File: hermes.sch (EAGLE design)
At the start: 17 parts, among them IC1 LP5912-WSON-6

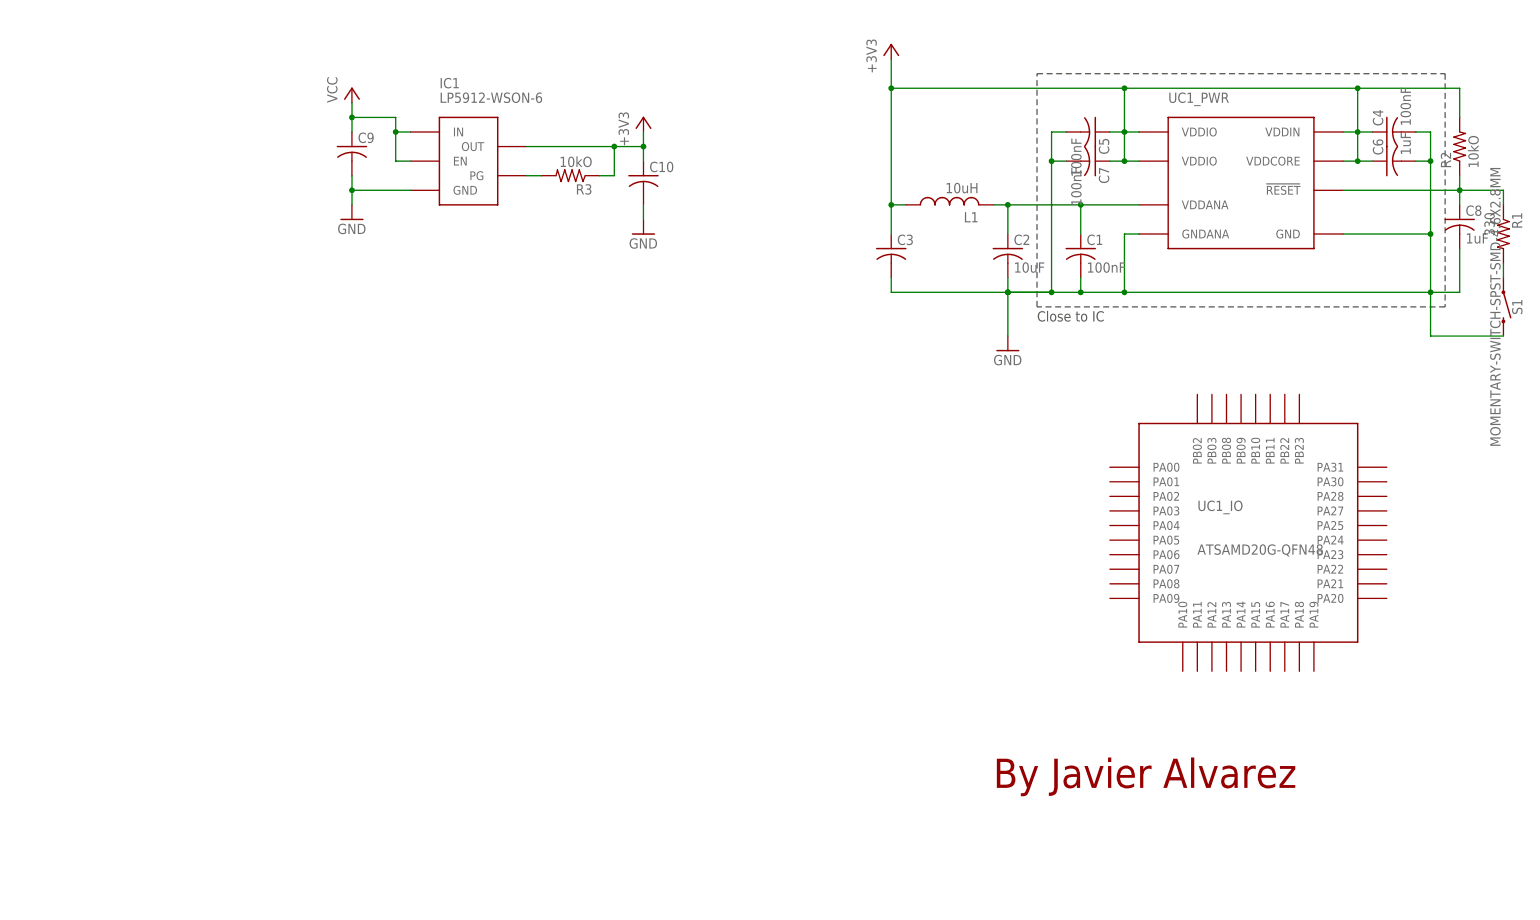
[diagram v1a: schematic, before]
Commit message: -SCH: Add placeholders for XTAL and LED -LBR: Add symbolic connection
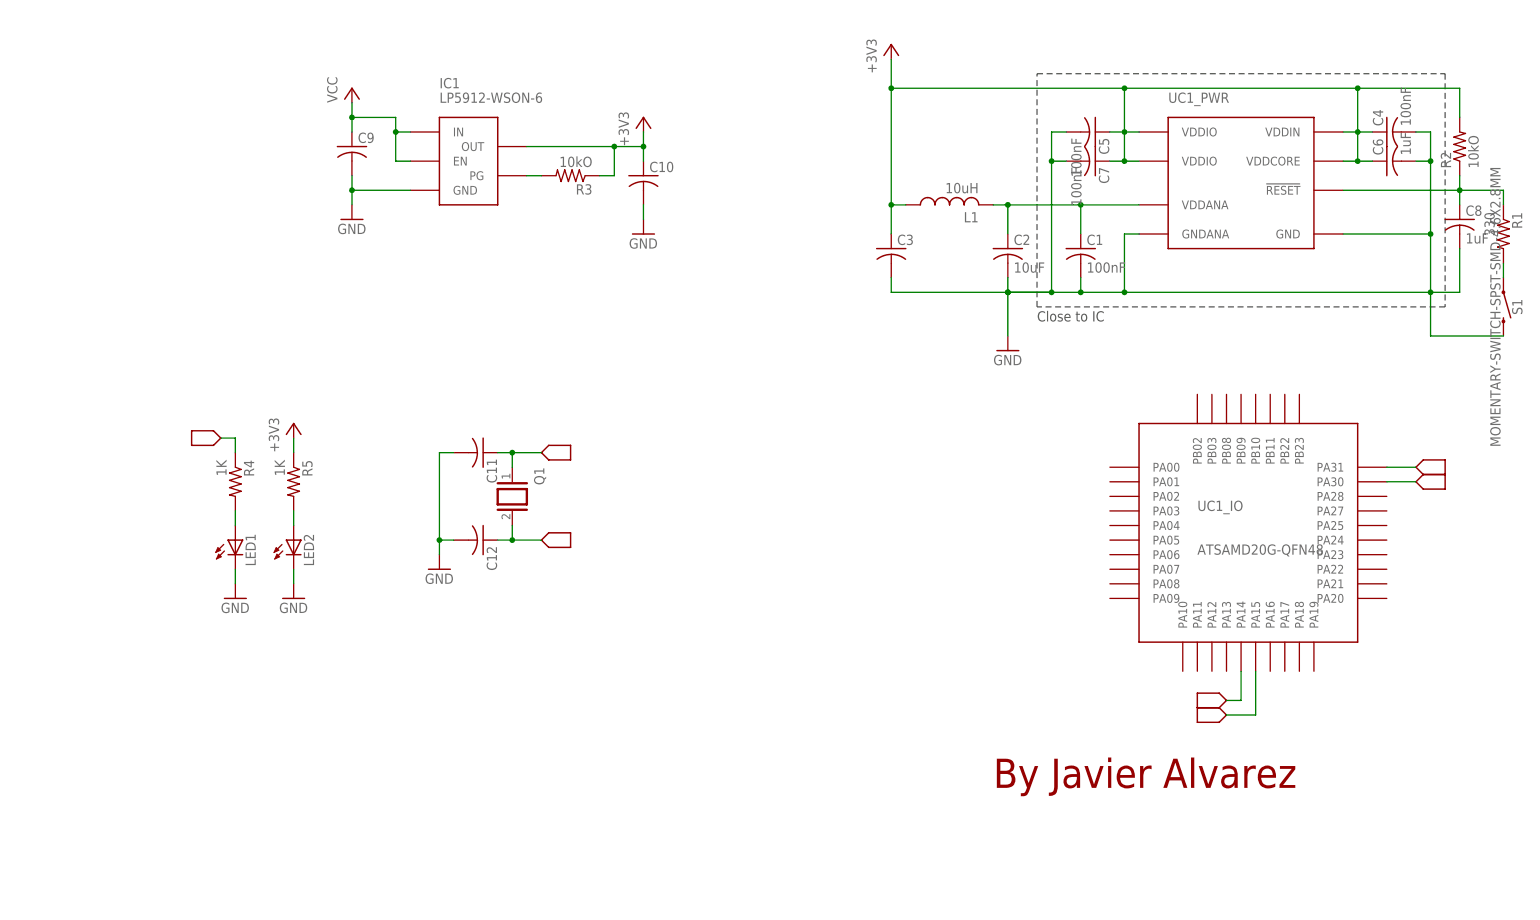
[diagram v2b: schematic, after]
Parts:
- added C11, C12: (no value), rcl:C-USC0201
- added LED1, LED2: (no value), eagle-ltspice:LED_ESML0603
- added Q1: (no value), special:XTAL
- added R4, R5: 1K, rcl:R-US_R0201
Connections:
- new net LED: R4.1
- new net N$6: LED1.A, R4.2
- new net N$7: LED2.A, R5.2
- new net SWCLK: UC1_IO.PA30
- new net SWDIO: UC1_IO.PA31
- new net XIN: C11.1, Q1.1, UC1_IO.PA14
- new net XOUT: C12.1, Q1.2, UC1_IO.PA15
- net +3V3: now also R5.1
- net GND: now also C11.2, C12.2, LED1.C, LED2.C
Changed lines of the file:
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@@
 <?xml version="1.0" encoding="utf-8"?>
 <!DOCTYPE eagle SYSTEM "eagle.dtd">
-<eagle version="8.3.0">
+<eagle version="8.5.0">
 <drawing>
 <settings>
@@
 <layer number="94" name="Symbols" color="4" fill="1" visible="yes" active="yes"/>
 <layer number="95" name="Names" color="7" fill="1" visible="yes" active="yes"/>
-<layer number="96" name="Values" color="7" fill="1" visible="no" active="yes"/>
+<layer number="96" name="Values" color="7" fill="1" visible="yes" active="yes"/>
 <layer number="97" name="Info" color="7" fill="1" visible="yes" active="yes"/>
 <layer number="98" name="Guide" color="6" fill="1" visible="yes" active="yes"/>
@@
 <part name="GND3" library="supply1" library_urn="urn:adsk.eagle:library:371" deviceset="GND" device=""/>
 <part name="+3V2" library="supply1" library_urn="urn:adsk.eagle:library:371" deviceset="+3V3" device=""/>
+<part name="U$1" library="Hermes_lib" deviceset="NET_CON" device=""/>
+<part name="LED1" library="eagle-ltspice" library_urn="urn:adsk.eagle:library:217" deviceset="LED_E" device="SML0603" package3d_urn="urn:adsk.eagle:package:13315/1"/>
+<part name="LED2" library="eagle-ltspice" library_urn="urn:adsk.eagle:library:217" deviceset="LED_E" device="SML0603" package3d_urn="urn:adsk.eagle:package:13315/1"/>
+<part name="R4" library="rcl" library_urn="urn:adsk.eagle:library:334" deviceset="R-US_" device="R0201" package3d_urn="urn:adsk.eagle:package:23593/1" value="1K"/>
+<part name="R5" library="rcl" library_urn="urn:adsk.eagle:library:334" deviceset="R-US_" device="R0201" package3d_urn="urn:adsk.eagle:package:23593/1" value="1K"/>
+<part name="+3V3" library="supply1" library_urn="urn:adsk.eagle:library:371" deviceset="+3V3" device=""/>
+<part name="GND4" library="supply1" library_urn="urn:adsk.eagle:library:371" deviceset="GND" device=""/>
+<part name="GND5" library="supply1" library_urn="urn:adsk.eagle:library:371" deviceset="GND" device=""/>
+<part name="Q1" library="special" library_urn="urn:adsk.eagle:library:367" deviceset="XTAL" device="" package3d_urn="urn:adsk.eagle:package:26649/1"/>
+<part name="U$2" library="Hermes_lib" deviceset="NET_CON" device=""/>
+<part name="U$3" library="Hermes_lib" deviceset="NET_CON" device=""/>
+<part name="C11" library="rcl" library_urn="urn:adsk.eagle:library:334" deviceset="C-US" device="C0201" package3d_urn="urn:adsk.eagle:package:23690/1"/>
+<part name="C12" library="rcl" library_urn="urn:adsk.eagle:library:334" deviceset="C-US" device="C0201" package3d_urn="urn:adsk.eagle:package:23690/1"/>
+<part name="GND6" library="supply1" library_urn="urn:adsk.eagle:library:371" deviceset="GND" device=""/>
+<part name="U$4" library="Hermes_lib" deviceset="NET_CON" device=""/>
+<part name="U$5" library="Hermes_lib" deviceset="NET_CON" device=""/>
+<part name="U$6" library="Hermes_lib" deviceset="NET_CON" device=""/>
+<part name="U$7" library="Hermes_lib" deviceset="NET_CON" device=""/>
 </parts>
 <sheets>
@@
 <instance part="GND3" gate="1" x="55.88" y="127"/>
 <instance part="+3V2" gate="G$1" x="106.68" y="144.78"/>
+<instance part="U$1" gate="G$1" x="33.02" y="88.9" rot="R180"/>
+<instance part="LED1" gate="G$1" x="35.56" y="71.12"/>
+<instance part="LED2" gate="G$1" x="45.72" y="71.12"/>
+<instance part="R4" gate="G$1" x="35.56" y="81.28" rot="R270"/>
+<instance part="R5" gate="G$1" x="45.72" y="81.28" rot="R270"/>
+<instance part="+3V3" gate="G$1" x="45.72" y="91.44"/>
+<instance part="GND4" gate="1" x="45.72" y="60.96"/>
+<instance part="GND5" gate="1" x="35.56" y="60.96"/>
+<instance part="Q1" gate="G$1" x="83.82" y="78.74" rot="R270"/>
+<instance part="U$2" gate="G$1" x="88.9" y="86.36"/>
+<instance part="U$3" gate="G$1" x="88.9" y="71.12"/>
+<instance part="C11" gate="G$1" x="78.74" y="86.36" rot="R270"/>
+<instance part="C12" gate="G$1" x="78.74" y="71.12" rot="R270"/>
+<instance part="GND6" gate="1" x="71.12" y="66.04"/>
+<instance part="U$4" gate="G$1" x="208.28" y="43.18" rot="R180"/>
+<instance part="U$5" gate="G$1" x="208.28" y="40.64" rot="R180"/>
+<instance part="U$6" gate="G$1" x="241.3" y="83.82"/>
+<instance part="U$7" gate="G$1" x="241.3" y="81.28"/>
 </instances>
 <busses>
@@
 <wire x1="106.68" y1="142.24" x2="106.68" y2="139.7" width="0.1524" layer="91"/>
 <junction x="106.68" y="139.7"/>
+</segment>
+<segment>
+<pinref part="R5" gate="G$1" pin="1"/>
+<pinref part="+3V3" gate="G$1" pin="+3V3"/>
+<wire x1="45.72" y1="86.36" x2="45.72" y2="88.9" width="0.1524" layer="91"/>
 </segment>
 </net>
@@
 <junction x="55.88" y="132.08"/>
 </segment>
+<segment>
+<pinref part="GND5" gate="1" pin="GND"/>
+<pinref part="LED1" gate="G$1" pin="C"/>
+<wire x1="35.56" y1="63.5" x2="35.56" y2="66.04" width="0.1524" layer="91"/>
+</segment>
+<segment>
+<pinref part="GND4" gate="1" pin="GND"/>
+<pinref part="LED2" gate="G$1" pin="C"/>
+<wire x1="45.72" y1="63.5" x2="45.72" y2="66.04" width="0.1524" layer="91"/>
+</segment>
+<segment>
+<pinref part="C11" gate="G$1" pin="2"/>
+<wire x1="73.66" y1="86.36" x2="71.12" y2="86.36" width="0.1524" layer="91"/>
+<wire x1="71.12" y1="86.36" x2="71.12" y2="71.12" width="0.1524" layer="91"/>
+<pinref part="C12" gate="G$1" pin="2"/>
+<wire x1="71.12" y1="71.12" x2="73.66" y2="71.12" width="0.1524" layer="91"/>
+<pinref part="GND6" gate="1" pin="GND"/>
+<wire x1="71.12" y1="68.58" x2="71.12" y2="71.12" width="0.1524" layer="91"/>
+<junction x="71.12" y="71.12"/>
+</segment>
 </net>
 <net name="N$2" class="0">
@@
 </segment>
 </net>
+<net name="LED" class="0">
+<segment>
+<pinref part="R4" gate="G$1" pin="1"/>
+<wire x1="35.56" y1="86.36" x2="35.56" y2="88.9" width="0.1524" layer="91"/>
+<wire x1="35.56" y1="88.9" x2="33.02" y2="88.9" width="0.1524" layer="91"/>
+</segment>
+</net>
+<net name="N$6" class="0">
+<segment>
+<pinref part="LED1" gate="G$1" pin="A"/>
+<pinref part="R4" gate="G$1" pin="2"/>
+<wire x1="35.56" y1="73.66" x2="35.56" y2="76.2" width="0.1524" layer="91"/>
+</segment>
+</net>
+<net name="N$7" class="0">
+<segment>
+<pinref part="LED2" gate="G$1" pin="A"/>
+<pinref part="R5" gate="G$1" pin="2"/>
+<wire x1="45.72" y1="73.66" x2="45.72" y2="76.2" width="0.1524" layer="91"/>
+</segment>
+</net>
+<net name="XIN" class="0">
+<segment>
+<pinref part="Q1" gate="G$1" pin="1"/>
+<wire x1="83.82" y1="86.36" x2="83.82" y2="83.82" width="0.1524" layer="91"/>
+<pinref part="C11" gate="G$1" pin="1"/>
+<wire x1="81.28" y1="86.36" x2="83.82" y2="86.36" width="0.1524" layer="91"/>
+<junction x="83.82" y="86.36"/>
+<wire x1="88.9" y1="86.36" x2="83.82" y2="86.36" width="0.1524" layer="91"/>
+</segment>
+<segment>
+<pinref part="UC1" gate="_IO" pin="PA14"/>
+<wire x1="210.82" y1="48.26" x2="210.82" y2="43.18" width="0.1524" layer="91"/>
+<wire x1="210.82" y1="43.18" x2="208.28" y2="43.18" width="0.1524" layer="91"/>
+</segment>
+</net>
+<net name="XOUT" class="0">
+<segment>
+<pinref part="Q1" gate="G$1" pin="2"/>
+<wire x1="88.9" y1="71.12" x2="83.82" y2="71.12" width="0.1524" layer="91"/>
+<wire x1="83.82" y1="71.12" x2="83.82" y2="73.66" width="0.1524" layer="91"/>
+<pinref part="C12" gate="G$1" pin="1"/>
+<wire x1="81.28" y1="71.12" x2="83.82" y2="71.12" width="0.1524" layer="91"/>
+<junction x="83.82" y="71.12"/>
+</segment>
+<segment>
+<pinref part="UC1" gate="_IO" pin="PA15"/>
+<wire x1="213.36" y1="48.26" x2="213.36" y2="40.64" width="0.1524" layer="91"/>
+<wire x1="213.36" y1="40.64" x2="208.28" y2="40.64" width="0.1524" layer="91"/>
+</segment>
+</net>
+<net name="SWDIO" class="0">
+<segment>
+<pinref part="UC1" gate="_IO" pin="PA31"/>
+<wire x1="236.22" y1="83.82" x2="241.3" y2="83.82" width="0.1524" layer="91"/>
+</segment>
+</net>
+<net name="SWCLK" class="0">
+<segment>
+<pinref part="UC1" gate="_IO" pin="PA30"/>
+<wire x1="236.22" y1="81.28" x2="241.3" y2="81.28" width="0.1524" layer="91"/>
+</segment>
+</net>

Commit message: -Add I2C placeholders
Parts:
- added R10, R11, R6, R7, R8, R9: 1K, rcl:R-US_R0201
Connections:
- net N$2 renamed !RESET
- new net SERCOM0_SCL: UC1_IO.PA09
- new net SERCOM0_SDA: R6.1, UC1_IO.PA08
- new net SERCOM1_SCL: UC1_IO.PA17
- new net SERCOM1_SDA: R7.1, UC1_IO.PA16
- new net SERCOM2_SCL: UC1_IO.PA13
- new net SERCOM2_SDA: R8.1, UC1_IO.PA12
- new net SERCOM3_SCL: UC1_IO.PA23
- new net SERCOM3_SDA: R9.1, UC1_IO.PA22
- new net SERCOM4_SCL: UC1_IO.PB09
- new net SERCOM4_SDA: R10.1, UC1_IO.PB08
- new net SERCOM5_SCL: UC1_IO.PB03
- new net SERCOM5_SDA: R11.1, UC1_IO.PB02
- net +3V3: now also R10.2, R11.2, R6.2, R7.2, R8.2, R9.2
- net LED: now also UC1_IO.PA05
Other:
- note added: "Javier Alvarez"
- note removed: "By Javier Alvarez"

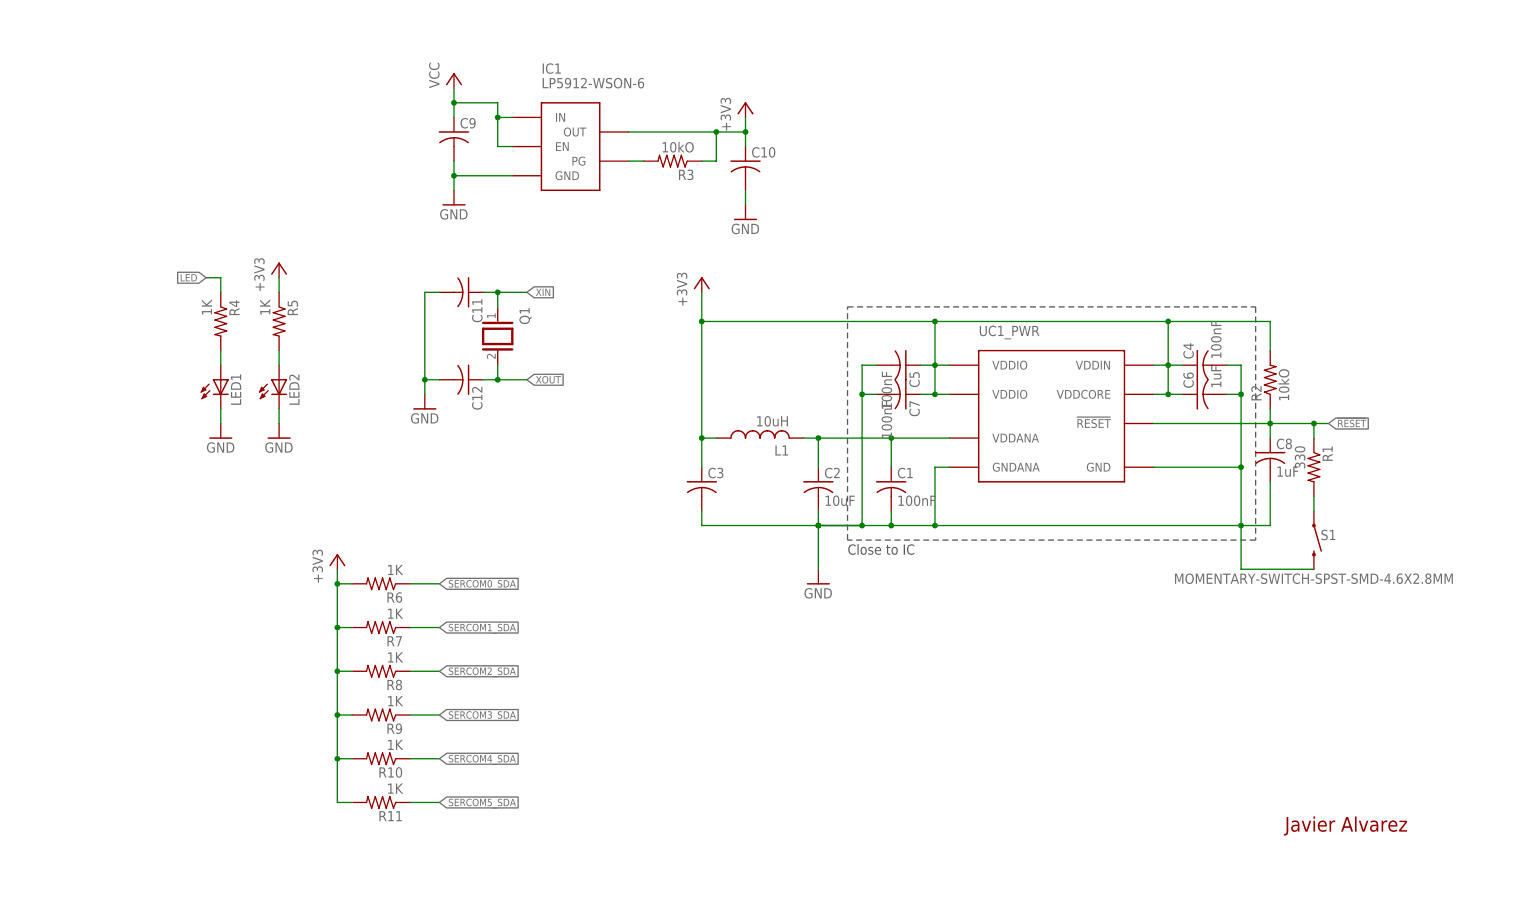
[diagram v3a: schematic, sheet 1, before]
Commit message: -Add XTAL to library -Add LDO to library -Add XTAL and LDO to schematics -Update .gitignore to ignore additional library files -Fix minor design flaws -Fix minor value errors in capacitance
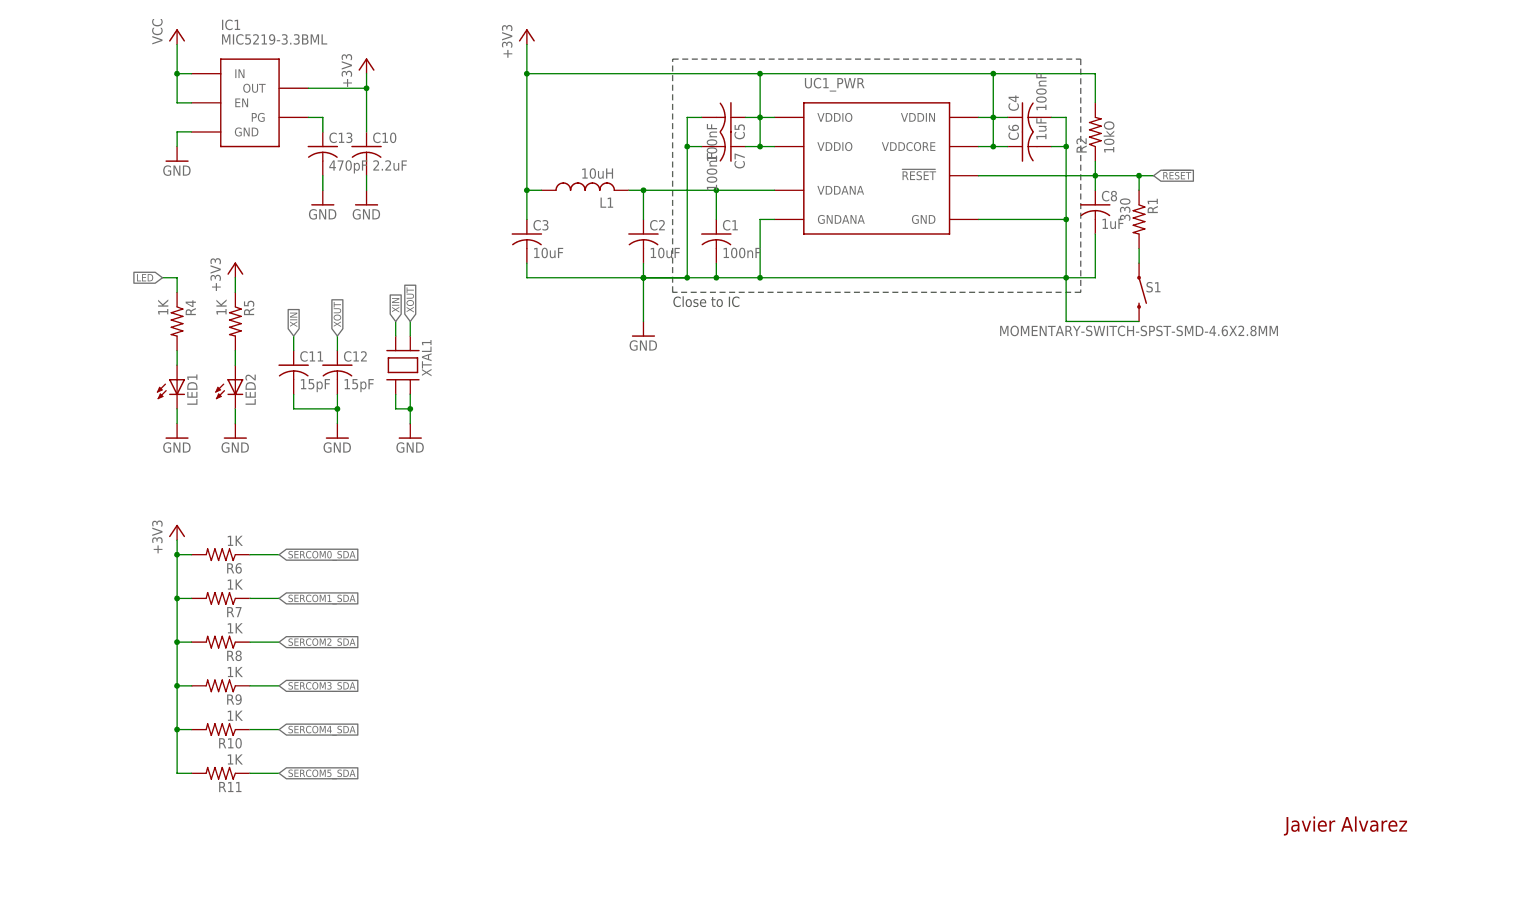
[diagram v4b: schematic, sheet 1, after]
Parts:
- removed C9: (no value), rcl:C-USC0201
- removed Q1: (no value), special:XTAL
- removed R3: 10kO, rcl:R-US_R0201
- added C13: 470pF, rcl:C-USC0201
- added XTAL1: (no value), Hermes_lib:LFXTAL059596CUTT
- C10: value (none) -> 2.2uF
- C11, C12: value (none) -> 15pF
- C3: value (none) -> 10uF
- IC1: value LP5912-WSON-6 -> MIC5219-3.3BML; device Hermes_lib:LP5912-WSON-6 -> Hermes_lib:MIC5219-3.3BML
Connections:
- removed net N$4: IC1.PG, R3.2
- new net N$2: C13.1, IC1.PG
- net +3V3: no longer R3.1
- net GND: now also C13.2, XTAL1.GND@1, XTAL1.GND@2; no longer C9.2
- net VCC: no longer C9.1
- net XIN: now also XTAL1.XTAL@1; no longer Q1.1
- net XOUT: now also XTAL1.XTAL@2; no longer Q1.2
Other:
- moved on the sheet: C1, C10, C11, C12, C2, C3, C4, C5, C6, C7, C8, IC1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
